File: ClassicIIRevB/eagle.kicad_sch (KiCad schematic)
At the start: 22 parts, among them U18 EAGLE

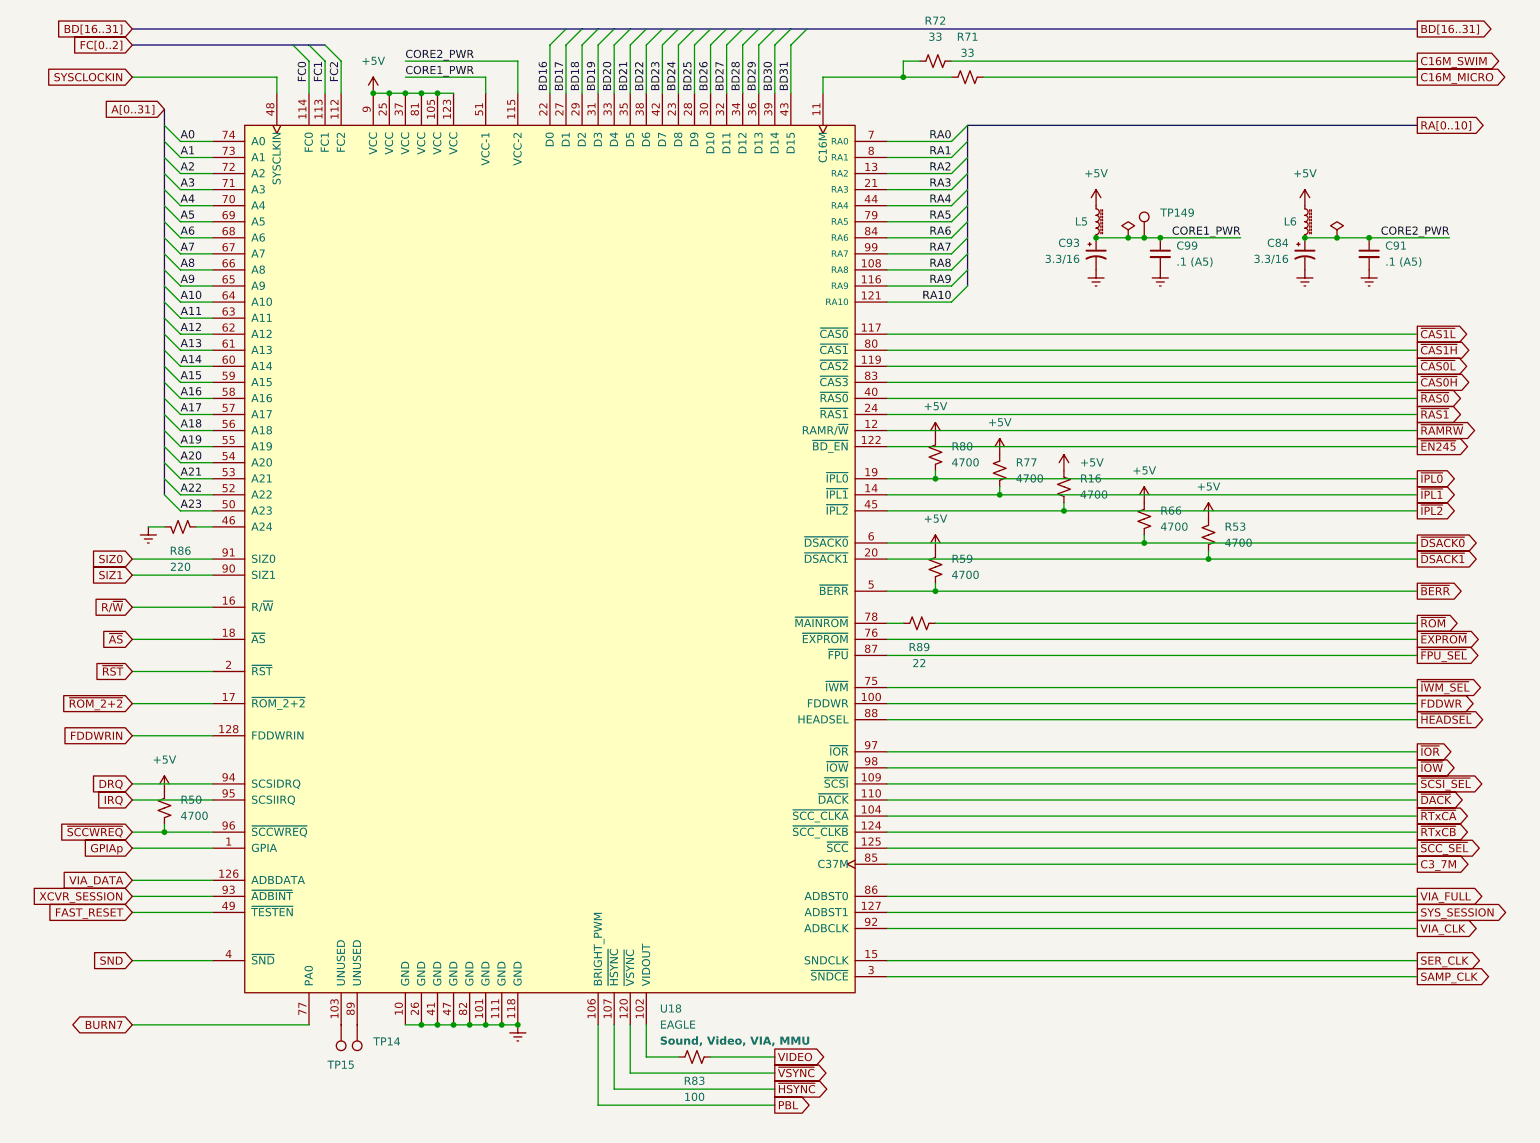
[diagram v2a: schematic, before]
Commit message: Switch to some "official" net names
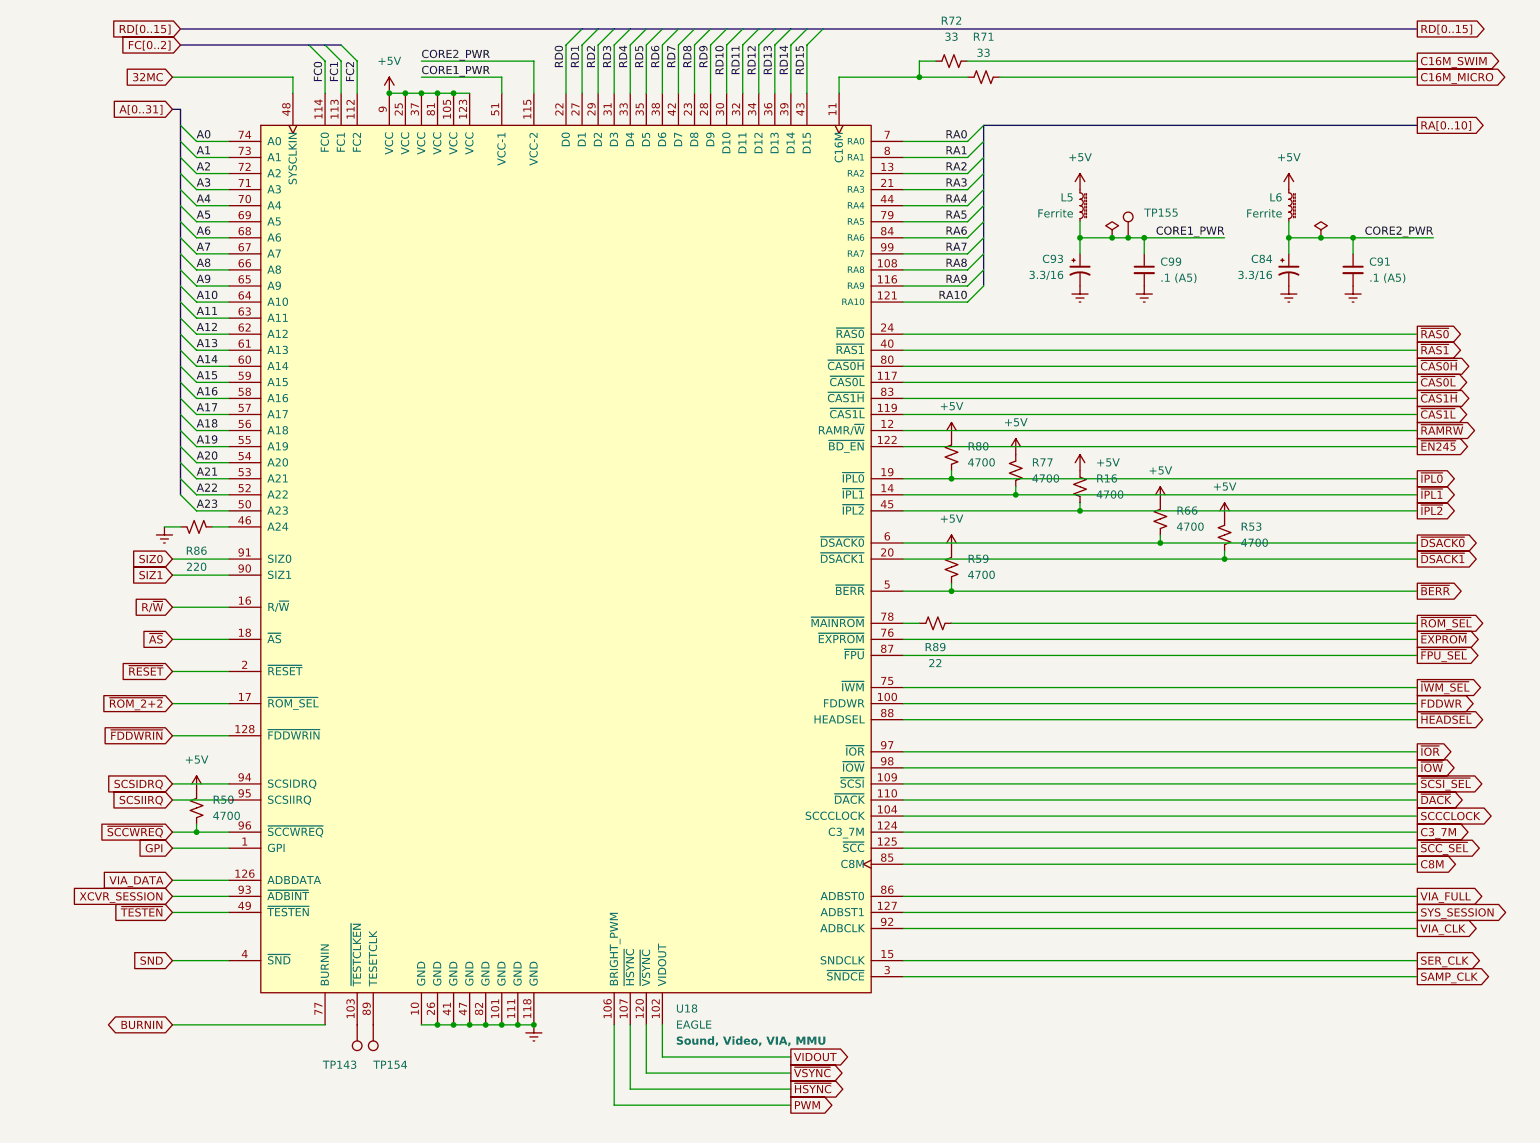
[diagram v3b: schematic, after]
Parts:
- removed R83: 100, MyPackage:SMD_0805_2012Metric_Pad1.25x1.65mm, symbol Device:R_Small_US
- L5, L6: value L_Ferrite_Small -> Ferrite
- renumbered TP15 to TP143, TP14 to TP154, TP149 to TP155
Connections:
- net ~{RTxCB} is gone; now on net C3_7M: U18.124 (C3_7M)
- net C3_7M: no longer U18.85 (C37M)
- net ~{CAS0H}: now also U18.80 (~{CAS0H}); no longer U18.83 (~{CAS3})
- net ~{CAS0L}: now also U18.117 (~{CAS0L}); no longer U18.119 (~{CAS2})
- net ~{CAS1H}: now also U18.83 (~{CAS1H}); no longer U18.80 (~{CAS1})
- net ~{CAS1L}: now also U18.119 (~{CAS1L}); no longer U18.117 (~{CAS0})
- net ~{RAS0}: now also U18.24 (~{RAS0}); no longer U18.40 (~{RAS0})
- net ~{RAS1}: now also U18.40 (~{RAS1}); no longer U18.24 (~{RAS1})
- net VIDOUT: now reaches U18.102 (VIDOUT)
- net BD16 renamed RD0
- net BD17 renamed RD1
- net BD18 renamed RD2
- net BD19 renamed RD3
- net BD20 renamed RD4
- net BD21 renamed RD5
- net BD22 renamed RD6
- net BD23 renamed RD7
- net BD24 renamed RD8
- net BD25 renamed RD9
- net BD26 renamed RD10
- net BD27 renamed RD11
- net BD28 renamed RD12
- net BD29 renamed RD13
- net BD30 renamed RD14
- net BD31 renamed RD15
- net BURN7 renamed BURNIN
- net DRQ renamed SCSIDRQ
- net FAST_RESET renamed ~{TESTEN}
- net FDDWRIN renamed ~{FDDWRIN}
- net GPIAp renamed GPI
- net IRQ renamed SCSIIRQ
- net PBL renamed PWM
- net SYSCLOCKIN renamed 32MC
- net ~{ROM} renamed ~{ROM_SEL}
- net ~{RST} renamed ~{RESET}
- net ~{RTxCA} renamed SCCCLOCK
- new net C8M: U18.85 (C8M)
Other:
- moved on the sheet: C84, C91, C93, C99, L5, L6, R16, R50, R53, R59, R66, R71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

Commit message: update exports
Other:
- title: Macintosh Classic II Revision B -> Macintosh Classic II (Later Revision)
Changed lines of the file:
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@@
 	(paper "USLetter")
 	(title_block
-		(title "Macintosh Classic II Revision B")
-		(date "2025-06-04")
+		(title "Macintosh Classic II (Later Revision)")
+		(date "2025-06-16")
 		(company "Apple Computer")
 		(comment 1 "drawn by Bradley Bell")

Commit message: Corrections to SMDs, more improved footprints
The later revision board reproduction design is now complete.
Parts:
- C84, C93: value 3.3/16 -> 3.3uF 16V
- C91, C99: value .1 (A5) -> 100nF
- R16, R50, R53, R59, R66, R77, R80: value 4700 -> 4.7K
- R71, R72: value 33 -> 33R
- R86: value 220 -> 220R
- R89: value 22 -> 22R
- TP143, TP154, TP155: now left out of the parts list
- U18: PartNum (none) -> 343S1054
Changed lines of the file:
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@@
 	(title_block
 		(title "Macintosh Classic II (Later Revision)")
-		(date "2025-06-16")
+		(date "2025-06-21")
 		(company "Apple Computer")
 		(comment 1 "drawn by Bradley Bell")
@@
 	(wire
 		(pts
-			(xy 121.92 180.34) (xy 121.92 175.26)
+			(xy 121.92 182.88) (xy 121.92 175.26)
 		)
 		(stroke
@@
 	(wire
 		(pts
-			(xy 116.84 185.42) (xy 116.84 175.26)
+			(xy 116.84 187.96) (xy 116.84 175.26)
 		)
 		(stroke
@@
 	(wire
 		(pts
-			(xy 142.24 185.42) (xy 116.84 185.42)
+			(xy 142.24 187.96) (xy 116.84 187.96)
 		)
 		(stroke
@@
 	(wire
 		(pts
-			(xy 142.24 187.96) (xy 114.3 187.96)
+			(xy 142.24 190.5) (xy 114.3 190.5)
 		)
 		(stroke
@@
 	(wire
 		(pts
-			(xy 142.24 182.88) (xy 119.38 182.88)
+			(xy 142.24 185.42) (xy 119.38 185.42)
 		)
 		(stroke
@@
 	(wire
 		(pts
-			(xy 114.3 187.96) (xy 114.3 175.26)
+			(xy 114.3 190.5) (xy 114.3 175.26)
 		)
 		(stroke
@@
 	(wire
 		(pts
-			(xy 119.38 182.88) (xy 119.38 175.26)
+			(xy 119.38 185.42) (xy 119.38 175.26)
 		)
 		(stroke
@@
 	(wire
 		(pts
-			(xy 121.92 180.34) (xy 142.24 180.34)
+			(xy 121.92 182.88) (xy 142.24 182.88)
 		)
 		(stroke
@@
 	(global_label "VIDOUT"
 		(shape output)
-		(at 142.24 180.34 0)
+		(at 142.24 182.88 0)
 		(fields_autoplaced yes)
 		(effects
@@
 		)
 		(property "Intersheetrefs" "${INTERSHEET_REFS}"
-			(at 151.8172 180.34 0)
+			(at 151.8172 182.88 0)
 			(effects
 				(font
@@
 	(global_label "~{VSYNC}"
 		(shape output)
-		(at 142.24 182.88 0)
+		(at 142.24 185.42 0)
 		(fields_autoplaced yes)
 		(effects
@@
 		)
 		(property "Intersheetrefs" "${INTERSHEET_REFS}"
-			(at 151.2124 182.88 0)
+			(at 151.2124 185.42 0)
 			(effects
 				(font
@@
 	(global_label "~{HSYNC}"
 		(shape output)
-		(at 142.24 185.42 0)
+		(at 142.24 187.96 0)
 		(fields_autoplaced yes)
 		(effects
@@
 		)
 		(property "Intersheetrefs" "${INTERSHEET_REFS}"
-			(at 151.4543 185.42 0)
+			(at 151.4543 187.96 0)
 			(effects
 				(font
@@
 	(global_label "PWM"
 		(shape output)
-		(at 142.24 187.96 0)
+		(at 142.24 190.5 0)
 		(fields_autoplaced yes)
 		(effects
@@
 		)
 		(property "Intersheetrefs" "${INTERSHEET_REFS}"
-			(at 149.398 187.96 0)
+			(at 149.398 190.5 0)
 			(effects
 				(font
@@
 			)
 		)
-		(property "Value" "4700"
+		(property "Value" "4.7K"
 			(at 170.18 104.1399 0)
 			(effects
@@
 			)
 		)
-		(property "Value" "4700"
+		(property "Value" "4.7K"
 			(at 180.34 88.8999 0)
 			(effects
@@
 		(on_board yes)
 		(dnp no)
-		(fields_autoplaced yes)
 		(property "Reference" "C84"
-			(at 218.44 54.1781 0)
+			(at 219.202 56.896 0)
 			(effects
 				(font
@@
 			)
 		)
-		(property "Value" "3.3/16"
-			(at 218.44 56.7181 0)
+		(property "Value" "3.3uF 16V"
+			(at 219.202 59.436 0)
 			(effects
 				(font
@@
 		(unit 1)
 		(exclude_from_sim no)
-		(in_bom yes)
+		(in_bom no)
 		(on_board yes)
 		(dnp no)
@@
 			)
 		)
-		(property "Value" "22"
+		(property "Value" "22R"
 			(at 165.1 118.11 90)
 			(effects
@@
 			)
 		)
-		(property "Value" "4700"
+		(property "Value" "4.7K"
 			(at 203.2 96.5199 0)
 			(effects
@@
 		(unit 1)
 		(exclude_from_sim no)
-		(in_bom yes)
+		(in_bom no)
 		(on_board yes)
 		(dnp no)
@@
 			)
 		)
-		(property "Value" "4700"
+		(property "Value" "4.7K"
 			(at 190.5 91.4399 0)
 			(effects
@@
 			)
 		)
-		(property "Value" "33"
+		(property "Value" "33R"
 			(at 167.64 19.05 90)
 			(effects
@@
 			)
 		)
+		(property "PartNum" "343S1054"
+			(at 124.0633 180.34 0)
+			(effects
+				(font
+					(size 1.27 1.27)
+				)
+				(justify left)
+			)
+		)
 		(pin "33"
 		)
@@
 			)
 		)
-		(property "Value" ".1 (A5)"
+		(property "Value" "100nF"
 			(at 233.68 57.1562 0)
 			(effects
@@
 			)
 		)
-		(property "Value" "3.3/16"
+		(property "Value" "3.3uF 16V"
 			(at 185.42 56.7181 0)
 			(effects
@@
 			)
 		)
-		(property "Value" "4700"
+		(property "Value" "4.7K"
 			(at 170.18 86.3599 0)
 			(effects
@@
 		(on_board yes)
 		(dnp no)
-		(fields_autoplaced yes)
 		(property "Reference" "C99"
-			(at 200.66 54.6162 0)
+			(at 200.152 53.086 0)
 			(effects
 				(font
@@
 			)
 		)
-		(property "Value" ".1 (A5)"
-			(at 200.66 57.1562 0)
+		(property "Value" "100nF"
+			(at 200.152 55.626 0)
 			(effects
 				(font
@@
 		(unit 1)
 		(exclude_from_sim no)
-		(in_bom yes)
+		(in_bom no)
 		(on_board yes)
 		(dnp no)
@@
 			)
 		)
-		(property "Value" "4700"
+		(property "Value" "4.7K"
 			(at 213.36 99.0599 0)
 			(effects
@@
 			)
 		)
-		(property "Value" "33"
+		(property "Value" "33R"
 			(at 172.72 21.59 90)
 			(effects
@@
 			)
 		)
-		(property "Value" "4700"
+		(property "Value" "4.7K"
 			(at 50.8 142.2399 0)
 			(effects
@@
 			)
 		)
-		(property "Value" "220"
+		(property "Value" "220R"
 			(at 48.26 102.87 90)
 			(effects
